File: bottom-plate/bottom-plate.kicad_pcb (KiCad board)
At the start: 2 copper layers, 81.8 x 57.2 mm, 4 parts

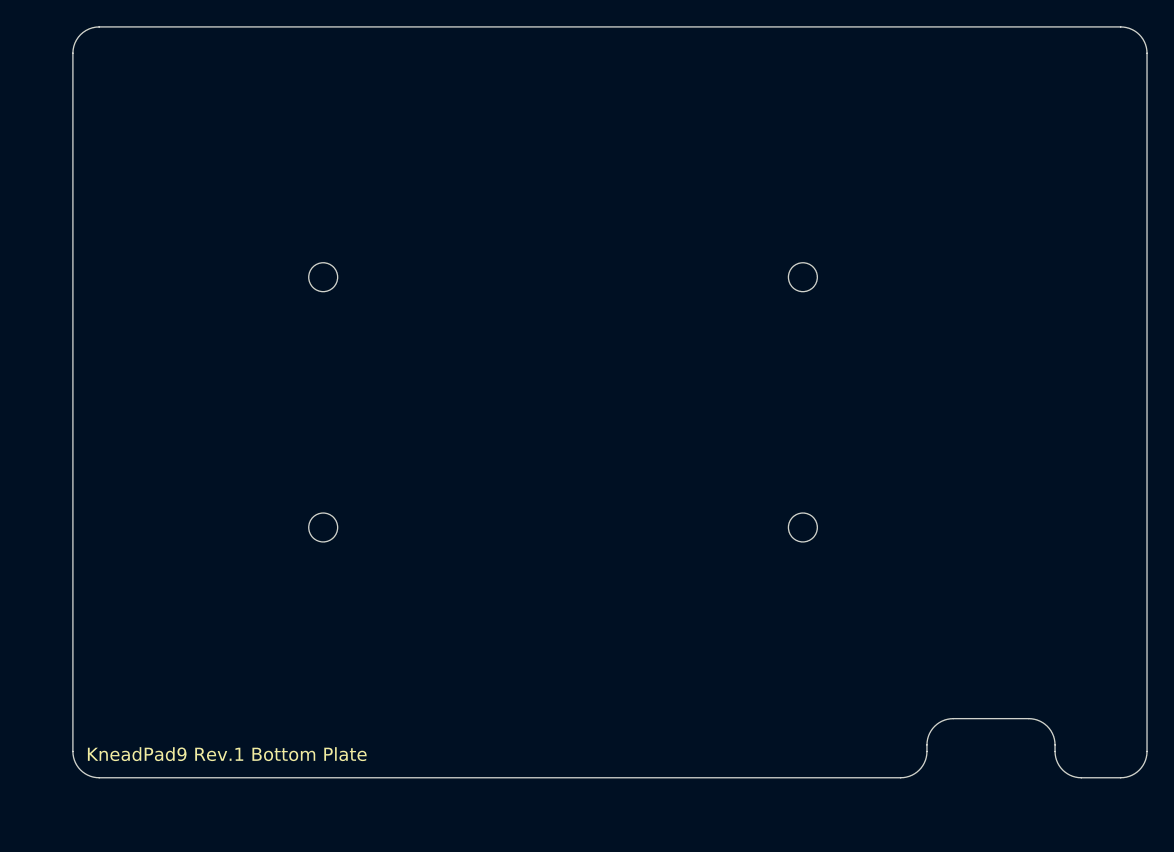
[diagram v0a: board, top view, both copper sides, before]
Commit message: added logo on bottom plate
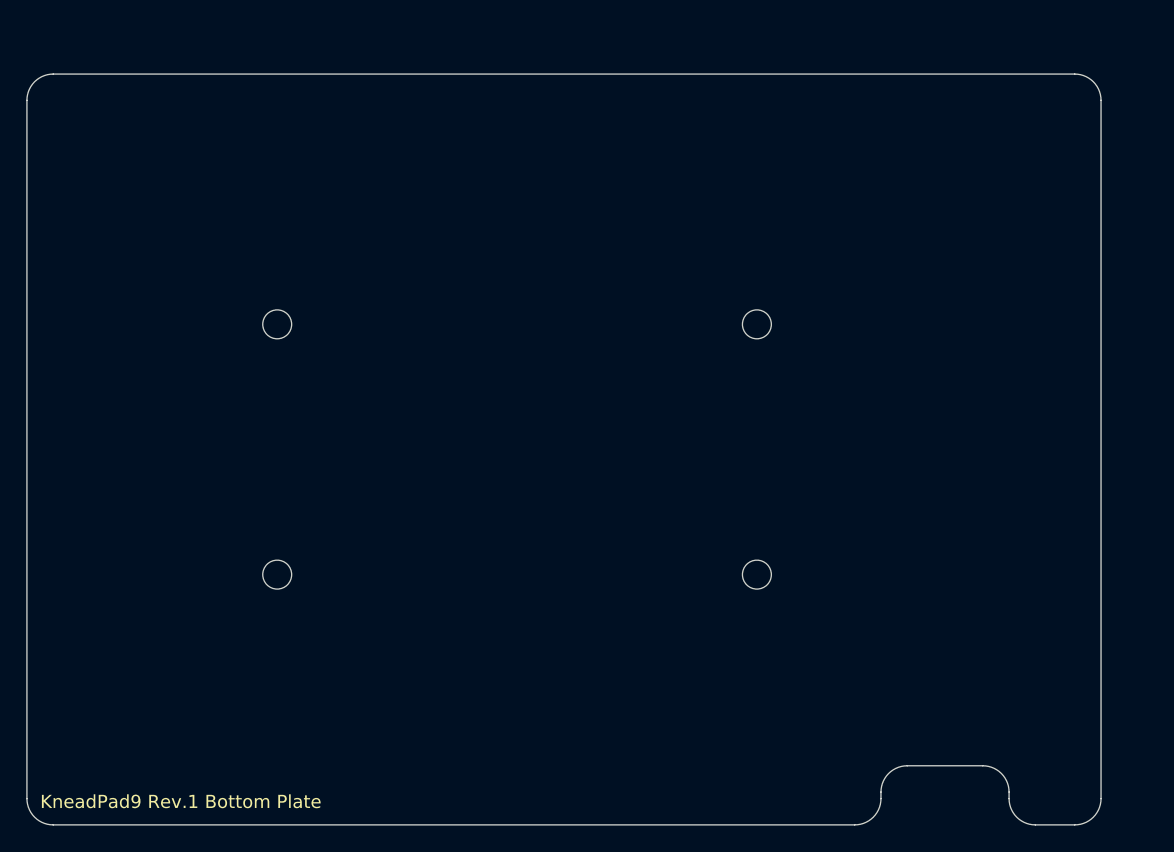
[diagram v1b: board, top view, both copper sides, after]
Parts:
- added G***: LOGO, LOGO, F.Cu at (149.6, 100.0)
- moved REF** 5.01 mm to (164.3, 109.5)
- moved REF** 5.01 mm to (164.3, 90.5)
- moved REF** 5.01 mm to (127.8, 90.5)
- moved REF** 5.01 mm to (127.8, 109.5)

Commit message: Add placeholder label for JLC order
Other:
- board text added: "JLCJLCJLCJLC"
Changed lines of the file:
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@@
       (layerselection 0x00010fc_ffffffff)
       (disableapertmacros false)
-      (usegerberextensions false)
+      (usegerberextensions true)
       (usegerberattributes true)
       (usegerberadvancedattributes true)
-      (creategerberjobfile true)
+      (creategerberjobfile false)
       (svguseinch false)
       (svgprecision 6)
@@
       (psa4output false)
       (plotreference true)
-      (plotvalue true)
+      (plotvalue false)
       (plotinvisibletext false)
       (sketchpadsonfab false)
@@
       (outputformat 1)
       (mirror false)
-      (drillshape 1)
+      (drillshape 0)
       (scaleselection 1)
-      (outputdirectory "")
+      (outputdirectory "gerber")
     )
   )
@@
   (gr_arc (start 190.5 126.5875) (mid 189.914214 128.001714) (end 188.5 128.5875) (layer "Edge.Cuts") (width 0.1))
   (gr_line (start 175.75 124.0875) (end 181.5 124.0875) (layer "Edge.Cuts") (width 0.1))
+  (gr_text "JLCJLCJLCJLC" (at 189.70625 73.025) (layer "F.SilkS")
+    (effects (font (size 1 1) (thickness 0.15)) (justify right))
+  )
   (gr_text "KneadPad9 Rev.1 Bottom Plate" (at 109.75 126.8375) (layer "F.SilkS")
     (effects (font (size 1 1) (thickness 0.125)) (justify left))
